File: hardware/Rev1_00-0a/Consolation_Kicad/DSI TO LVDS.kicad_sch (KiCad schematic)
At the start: 27 parts, among them Q10 SSM3K56FS,LF, Q11 SSM3K56FS,LF, U15 SN65DSI84ZXHR, U16 SN74LVC1G125DBVR

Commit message: Add part number of codec to block diagram Add codec and hdmi schematic sheets
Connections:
- net 1V8_CB renamed 1V8
- net 3V3_CB renamed 3V3
- net I2C3.I2C_SCL renamed I2C2.I2C_SCL
- net I2C3.I2C_SDA renamed I2C2.I2C_SDA
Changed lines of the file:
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@@
 		)
 	)
-	(label "I2C3.I2C_SDA"
+	(label "I2C2.I2C_SDA"
 		(at 74.295 81.28 0)
 		(effects
@@
 		)
 	)
-	(label "I2C3.I2C_SCL"
+	(label "I2C2.I2C_SCL"
 		(at 74.295 97.155 0)
 		(effects
@@
 		)
 	)
-	(hierarchical_label "I2C3{I2C}"
+	(hierarchical_label "I2C2{I2C}"
 		(shape bidirectional)
 		(at 38.1 76.2 180)
@@
 	(symbol
 		(lib_id "KiCad_Pwr_Symbols:+3V3")
-		(at 125.095 120.015 0)
+		(at 136.525 96.52 90)
 		(unit 1)
 		(body_style 1)
@@
 		(in_pos_files yes)
 		(dnp no)
-		(property "Reference" "#PWR0124"
-			(at 125.095 123.825 0)
+		(property "Reference" "#PWR0145"
+			(at 140.335 96.52 0)
 			(hide yes)
 			(show_name no)
@@
 			)
 		)
-		(property "Value" "1V8_CB"
-			(at 121.158 116.459 0)
+		(property "Value" "1V8"
+			(at 133.858 96.52 90)
 			(show_name no)
 			(do_not_autoplace no)
@@
 		)
 		(property "Footprint" ""
-			(at 125.095 120.015 0)
+			(at 136.525 96.52 0)
 			(hide yes)
 			(show_name no)
@@
 		)
 		(property "Datasheet" ""
-			(at 125.095 120.015 0)
+			(at 136.525 96.52 0)
 			(hide yes)
 			(show_name no)
@@
 		)
 		(property "Description" "Power symbol creates a global label with name \"+3V3\""
-			(at 125.095 120.015 0)
+			(at 136.525 96.52 0)
 			(hide yes)
 			(show_name no)
@@
 			(project "Consolation_Kicad"
 				(path "/b18b5a64-cfe0-4447-acaf-556f3c6e6513/840a7f6c-235f-45c3-9d8a-e775048afd33"
-					(reference "#PWR0124")
+					(reference "#PWR0145")
 					(unit 1)
 				)
@@
 	)
 	(symbol
-		(lib_id "KiCad_Pwr_Symbols:+3V3")
-		(at 106.045 86.995 0)
-		(unit 1)
-		(body_style 1)
-		(exclude_from_sim no)
-		(in_bom yes)
-		(on_board yes)
-		(in_pos_files yes)
-		(dnp no)
-		(property "Reference" "#PWR0133"
-			(at 106.045 90.805 0)
-			(hide yes)
-			(show_name no)
-			(do_not_autoplace no)
-			(effects
-				(font
-					(size 1.27 1.27)
-				)
-			)
-		)
-		(property "Value" "1V8_CB"
-			(at 102.997 83.566 0)
-			(show_name no)
-			(do_not_autoplace no)
-			(effects
-				(font
-					(size 1.27 1.27)
-				)
-				(justify left)
-			)
-		)
-		(property "Footprint" ""
-			(at 106.045 86.995 0)
-			(hide yes)
-			(show_name no)
-			(do_not_autoplace no)
-			(effects
-				(font
-					(size 1.27 1.27)
-				)
-			)
-		)
-		(property "Datasheet" ""
-			(at 106.045 86.995 0)
-			(hide yes)
-			(show_name no)
-			(do_not_autoplace no)
-			(effects
-				(font
-					(size 1.27 1.27)
-				)
-			)
-		)
-		(property "Description" "Power symbol creates a global label with name \"+3V3\""
-			(at 106.045 86.995 0)
-			(hide yes)
-			(show_name no)
-			(do_not_autoplace no)
-			(effects
-				(font
-					(size 1.27 1.27)
-				)
-			)
-		)
-		(pin "1"
-		)
-		(instances
-			(project "Consolation_Kicad"
-				(path "/b18b5a64-cfe0-4447-acaf-556f3c6e6513/840a7f6c-235f-45c3-9d8a-e775048afd33"
-					(reference "#PWR0133")
-					(unit 1)
-				)
-			)
-		)
-	)
-	(symbol
 		(lib_id "KicadCompDb:Resistors/RES_SMT_00013")
 		(at 83.82 112.395 180)
@@
 			)
 		)
-		(property "Value" "3V3_CB"
+		(property "Value" "3V3"
 			(at 54.356 114.808 90)
 			(show_name no)
@@
 	)
 	(symbol
+		(lib_id "KiCad_Pwr_Symbols:+3V3")
+		(at 125.095 120.015 0)
+		(unit 1)
+		(body_style 1)
+		(exclude_from_sim no)
+		(in_bom yes)
+		(on_board yes)
+		(in_pos_files yes)
+		(dnp no)
+		(property "Reference" "#PWR0144"
+			(at 125.095 123.825 0)
+			(hide yes)
+			(show_name no)
+			(do_not_autoplace no)
+			(effects
+				(font
+					(size 1.27 1.27)
+				)
+			)
+		)
+		(property "Value" "1V8"
+			(at 123.19 116.459 0)
+			(show_name no)
+			(do_not_autoplace no)
+			(effects
+				(font
+					(size 1.27 1.27)
+				)
+				(justify left)
+			)
+		)
+		(property "Footprint" ""
+			(at 125.095 120.015 0)
+			(hide yes)
+			(show_name no)
+			(do_not_autoplace no)
+			(effects
+				(font
+					(size 1.27 1.27)
+				)
+			)
+		)
+		(property "Datasheet" ""
+			(at 125.095 120.015 0)
+			(hide yes)
+			(show_name no)
+			(do_not_autoplace no)
+			(effects
+				(font
+					(size 1.27 1.27)
+				)
+			)
+		)
+		(property "Description" "Power symbol creates a global label with name \"+3V3\""
+			(at 125.095 120.015 0)
+			(hide yes)
+			(show_name no)
+			(do_not_autoplace no)
+			(effects
+				(font
+					(size 1.27 1.27)
+				)
+			)
+		)
+		(pin "1"
+		)
+		(instances
+			(project "Consolation_Kicad"
+				(path "/b18b5a64-cfe0-4447-acaf-556f3c6e6513/840a7f6c-235f-45c3-9d8a-e775048afd33"
+					(reference "#PWR0144")
+					(unit 1)
+				)
+			)
+		)
+	)
+	(symbol
 		(lib_id "KicadCompDb:Resistors/RES_SMT_00001")
 		(at 139.7 96.52 0)
@@
 	)
 	(symbol
-		(lib_id "KiCad_Pwr_Symbols:+3V3")
-		(at 136.525 96.52 90)
-		(unit 1)
-		(body_style 1)
-		(exclude_from_sim no)
-		(in_bom yes)
-		(on_board yes)
-		(in_pos_files yes)
-		(dnp no)
-		(property "Reference" "#PWR0132"
-			(at 140.335 96.52 0)
-			(hide yes)
-			(show_name no)
-			(do_not_autoplace no)
-			(effects
-				(font
-					(size 1.27 1.27)
-				)
-			)
-		)
-		(property "Value" "1V8_CB"
-			(at 133.35 96.52 90)
-			(show_name no)
-			(do_not_autoplace no)
-			(effects
-				(font
-					(size 1.27 1.27)
-				)
-				(justify left)
-			)
-		)
-		(property "Footprint" ""
-			(at 136.525 96.52 0)
-			(hide yes)
-			(show_name no)
-			(do_not_autoplace no)
-			(effects
-				(font
-					(size 1.27 1.27)
-				)
-			)
-		)
-		(property "Datasheet" ""
-			(at 136.525 96.52 0)
-			(hide yes)
-			(show_name no)
-			(do_not_autoplace no)
-			(effects
-				(font
-					(size 1.27 1.27)
-				)
-			)
-		)
-		(property "Description" "Power symbol creates a global label with name \"+3V3\""
-			(at 136.525 96.52 0)
-			(hide yes)
-			(show_name no)
-			(do_not_autoplace no)
-			(effects
-				(font
-					(size 1.27 1.27)
-				)
-			)
-		)
-		(pin "1"
-		)
-		(instances
-			(project "Consolation_Kicad"
-				(path "/b18b5a64-cfe0-4447-acaf-556f3c6e6513/840a7f6c-235f-45c3-9d8a-e775048afd33"
-					(reference "#PWR0132")
-					(unit 1)
-				)
-			)
-		)
-	)
-	(symbol
 		(lib_id "KicadCompDb:Interface/INTRFX_00001")
 		(at 168.275 52.07 0)
@@
 			)
 		)
-		(property "Value" "3V3_CB"
-			(at 102.997 67.691 0)
+		(property "Value" "3V3"
+			(at 104.14 67.564 0)
 			(show_name no)
 			(do_not_autoplace no)
@@
 	)
 	(symbol
+		(lib_id "KiCad_Pwr_Symbols:+3V3")
+		(at 93.345 86.995 0)
+		(unit 1)
+		(body_style 1)
+		(exclude_from_sim no)
+		(in_bom yes)
+		(on_board yes)
+		(in_pos_files yes)
+		(dnp no)
+		(property "Reference" "#PWR0142"
+			(at 93.345 90.805 0)
+			(hide yes)
+			(show_name no)
+			(do_not_autoplace no)
+			(effects
+				(font
+					(size 1.27 1.27)
+				)
+			)
+		)
+		(property "Value" "3V3"
+			(at 91.44 83.439 0)
+			(show_name no)
+			(do_not_autoplace no)
+			(effects
+				(font
+					(size 1.27 1.27)
+				)
+				(justify left)
+			)
+		)
+		(property "Footprint" ""
+			(at 93.345 86.995 0)
+			(hide yes)
+			(show_name no)
+			(do_not_autoplace no)
+			(effects
+				(font
+					(size 1.27 1.27)
+				)
+			)
+		)
+		(property "Datasheet" ""
+			(at 93.345 86.995 0)
+			(hide yes)
+			(show_name no)
+			(do_not_autoplace no)
+			(effects
+				(font
+					(size 1.27 1.27)
+				)
+			)
+		)
+		(property "Description" "Power symbol creates a global label with name \"+3V3\""
+			(at 93.345 86.995 0)
+			(hide yes)
+			(show_name no)
+			(do_not_autoplace no)
+			(effects
+				(font
+					(size 1.27 1.27)
+				)
+			)
+		)
+		(pin "1"
+		)
+		(instances
+			(project "Consolation_Kicad"
+				(path "/b18b5a64-cfe0-4447-acaf-556f3c6e6513/840a7f6c-235f-45c3-9d8a-e775048afd33"
+					(reference "#PWR0142")
+					(unit 1)
+				)
+			)
+		)
+	)
+	(symbol
 		(lib_id "KicadCompDb:Capacitors/CAP_CER_SMT_00001")
 		(at 59.055 121.285 270)
@@
 	(symbol
 		(lib_id "KiCad_Pwr_Symbols:+3V3")
-		(at 93.345 86.995 0)
+		(at 106.045 86.995 0)
 		(unit 1)
 		(body_style 1)
@@
 		(in_pos_files yes)
 		(dnp no)
-		(property "Reference" "#PWR0134"
-			(at 93.345 90.805 0)
+		(property "Reference" "#PWR0143"
+			(at 106.045 90.805 0)
 			(hide yes)
 			(show_name no)
@@
 			)
 		)
-		(property "Value" "3V3_CB"
-			(at 90.297 83.566 0)
+		(property "Value" "1V8"
+			(at 104.14 83.439 0)
 			(show_name no)
 			(do_not_autoplace no)
@@
 		)
 		(property "Footprint" ""
-			(at 93.345 86.995 0)
+			(at 106.045 86.995 0)
 			(hide yes)
 			(show_name no)
@@
 		)
 		(property "Datasheet" ""
-			(at 93.345 86.995 0)
+			(at 106.045 86.995 0)
 			(hide yes)
 			(show_name no)
@@
 		)
 		(property "Description" "Power symbol creates a global label with name \"+3V3\""
-			(at 93.345 86.995 0)
+			(at 106.045 86.995 0)
 			(hide yes)
 			(show_name no)
@@
 			(project "Consolation_Kicad"
 				(path "/b18b5a64-cfe0-4447-acaf-556f3c6e6513/840a7f6c-235f-45c3-9d8a-e775048afd33"
-					(reference "#PWR0134")
+					(reference "#PWR0143")
 					(unit 1)
 				)
@@
 			)
 		)
-		(property "Value" "1V8_CB"
-			(at 115.697 67.691 0)
+		(property "Value" "1V8"
+			(at 116.84 67.564 0)
 			(show_name no)
 			(do_not_autoplace no)

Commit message: Update schematics, block diagram and pin mux (good progress G)
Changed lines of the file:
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@@
 	(text "Resistors are 1% 1/16W 0402 unless otherwise noted\nCapacitors are 10% 50V X7R 0402 unless otherwise noted"
 		(exclude_from_sim no)
-		(at 12.7 170.307 0)
+		(at 12.7 170.942 0)
 		(effects
 			(font

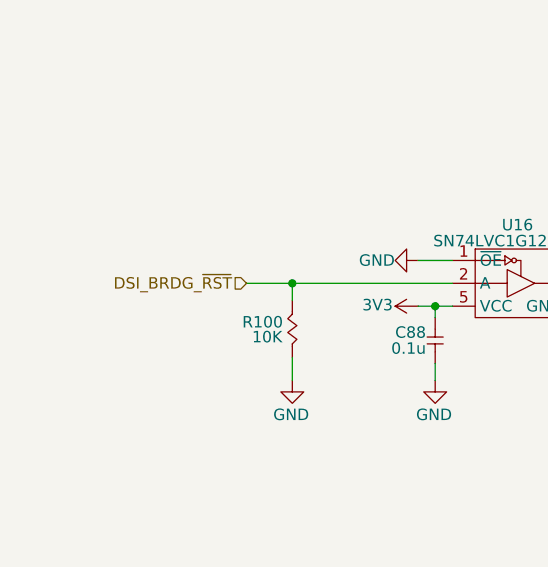
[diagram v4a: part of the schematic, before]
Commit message: Work on block diagram and top-level schematic sheet Work on PinMux
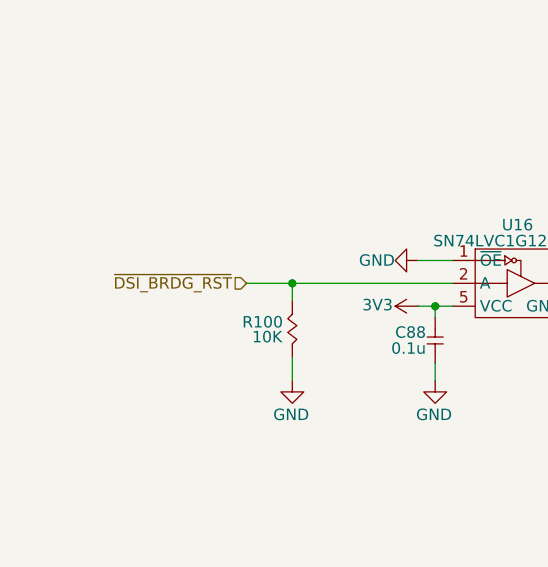
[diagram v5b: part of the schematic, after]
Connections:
- net DSI_BRDG_~{RST} renamed ~{DSI_BRDG_RST}
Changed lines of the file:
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@@
 		)
 	)
-	(hierarchical_label "DSI_BRDG_~{RST}"
+	(hierarchical_label "~{DSI_BRDG_RST}"
 		(shape input)
 		(at 38.1 112.395 180)
